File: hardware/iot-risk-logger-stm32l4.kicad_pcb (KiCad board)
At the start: 2 copper layers, 51 x 51 mm, 49 parts, among them J2 Conn_ST_STDC14, J3 USB Type-C, Q1 IRLML6401, U1 STM32L412K8Tx, U2 MMA8452QR1, U3 ST25DV04K, U4 OPT3001DNPR, U5 SHT30-DIS, U6 AT25SF041B-SSHD-T, U7 L78L33ABUTR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

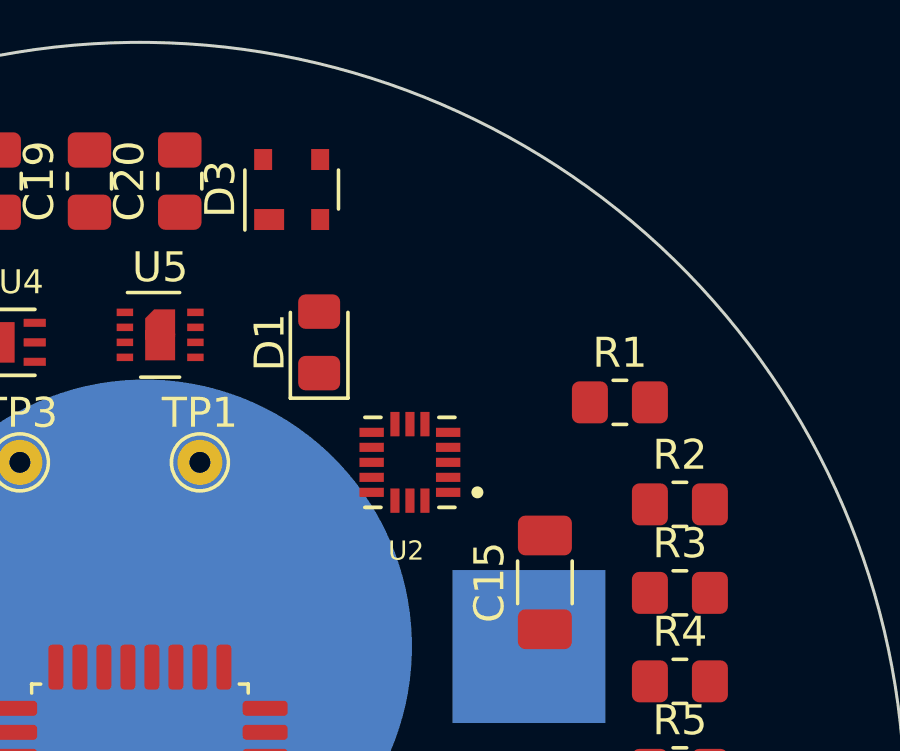
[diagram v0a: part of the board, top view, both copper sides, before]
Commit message: rename to iot-risk-logger-stm32l4 and andd harwware/
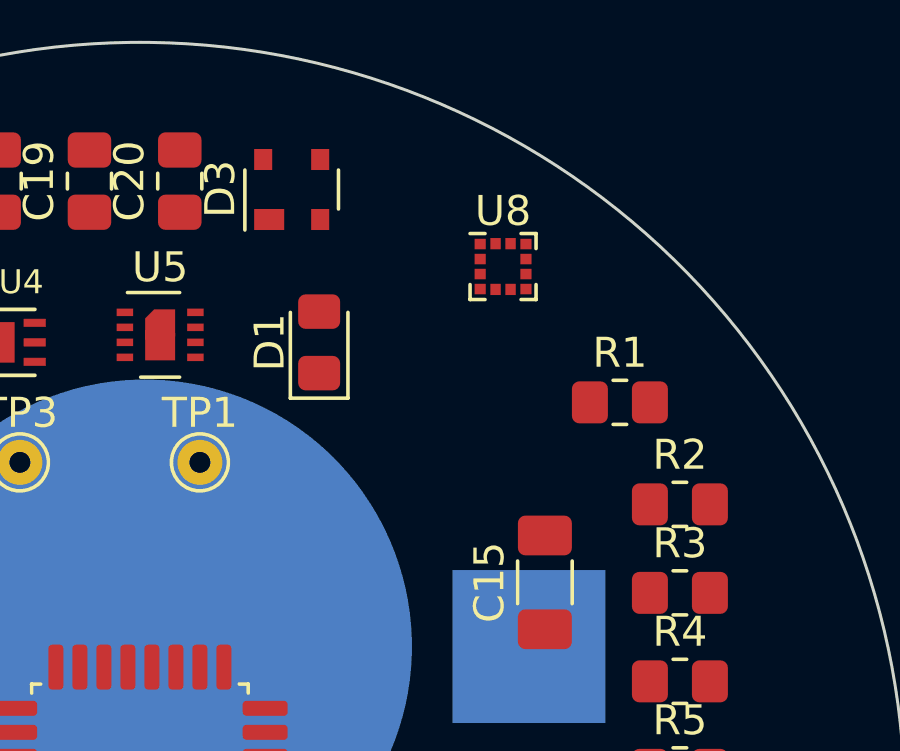
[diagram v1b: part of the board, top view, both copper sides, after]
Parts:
- removed U2: MMA8452QR1, Personal:XDCR_MMA8452QR1
- added U8: LIS2DW12, Package_LGA:LGA-12_2x2mm_P0.5mm, F.Cu at (141.6, 69.0)
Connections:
- C9 pad 1: Net-(U2-BYP) -> unconnected-(C9-Pad1)

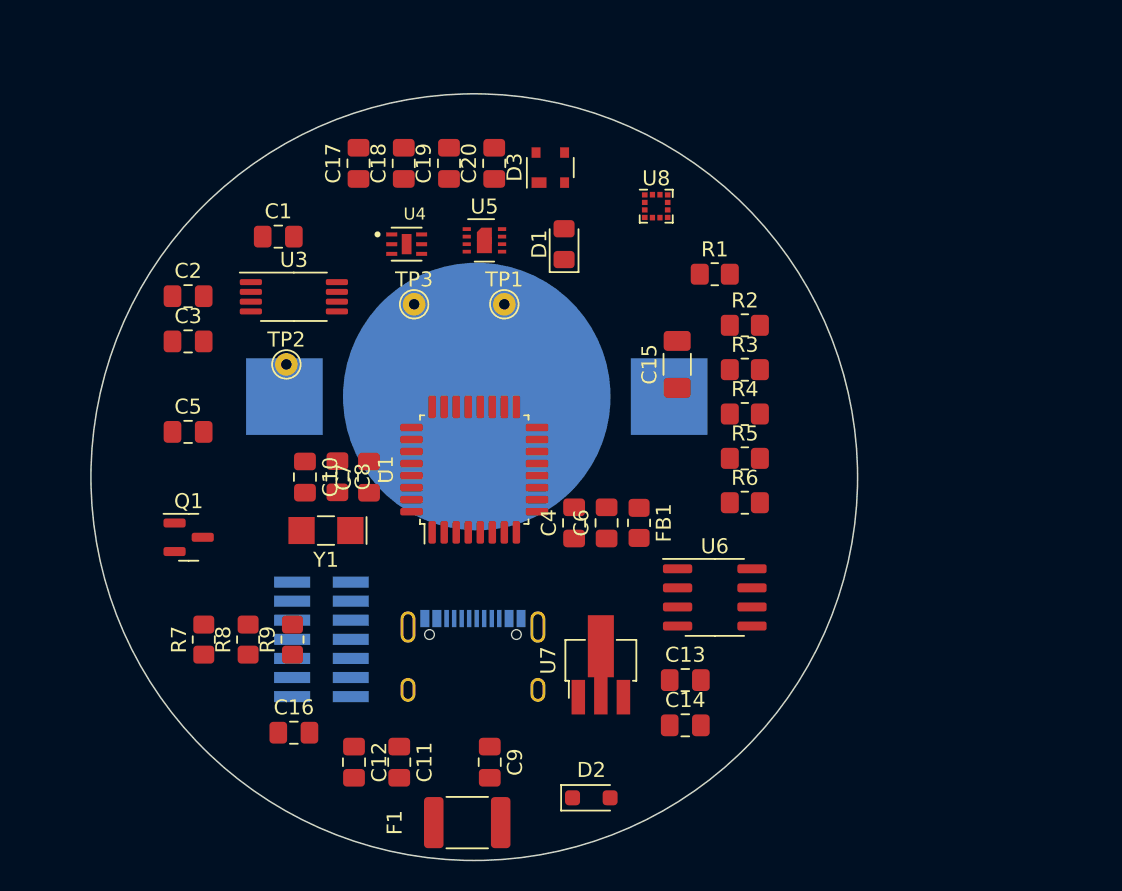
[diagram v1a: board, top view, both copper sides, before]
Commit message: CubeMX: set pins
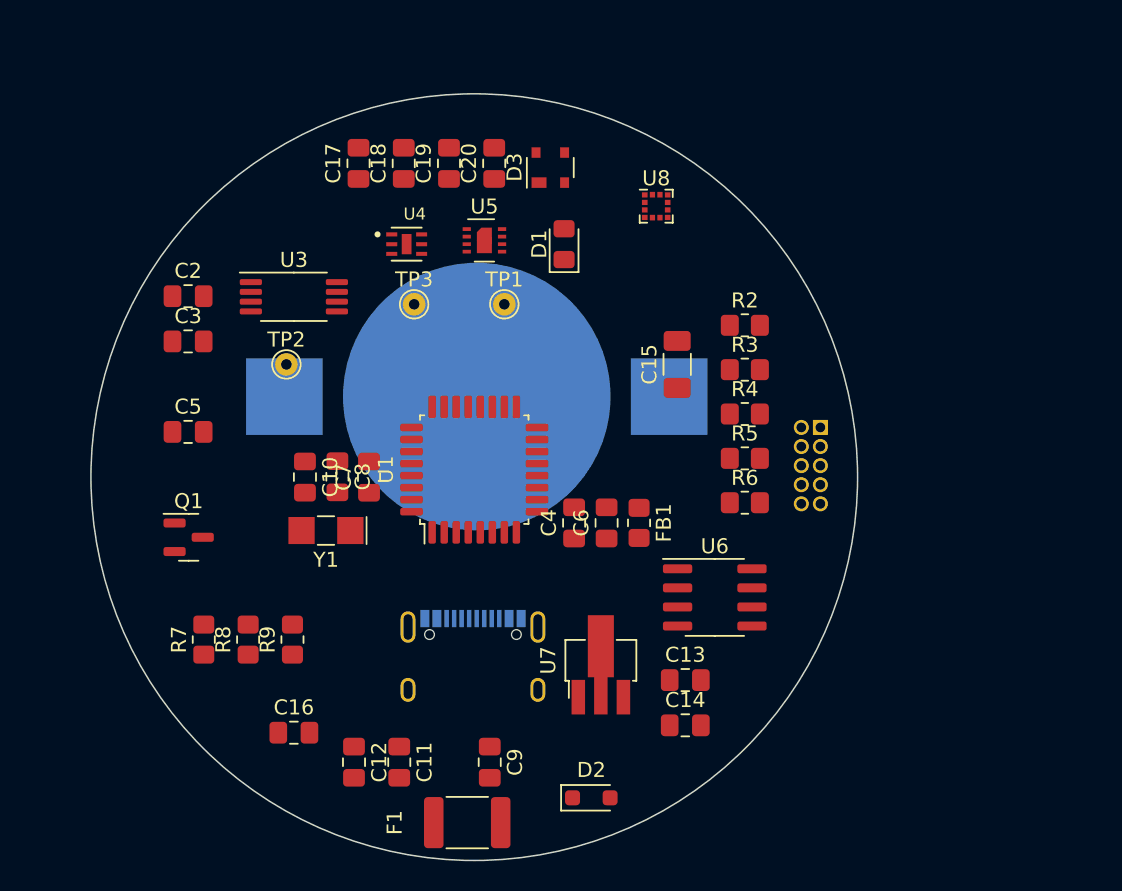
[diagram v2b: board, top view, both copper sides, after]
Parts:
- removed C1: 100n, Capacitor_SMD:C_0805_2012Metric_Pad1.18x1.45mm_HandSolder
- removed J2: Conn_ST_STDC14, Connector_PinHeader_1.27mm:PinHeader_2x07_P1.27mm_Vertical_SMD
- removed R1: 1k, Resistor_SMD:R_0805_2012Metric_Pad1.20x1.40mm_HandSolder
- added J1: Conn_ARM_JTAG_SWD_10, Connector_PinHeader_1.27mm:PinHeader_2x05_P1.27mm_Vertical, B.Cu at (152.5, 83.7)
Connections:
- C17 pad 1: XIN32 -> OSC32_IN
- C18 pad 1: XOUT32 -> OSC32_OUT
- U1 pad 10: unconnected-(U1-PA4-Pad10) -> IMU_INT2
- U1 pad 11: unconnected-(U1-PA5-Pad11) -> SCK
- U1 pad 12: unconnected-(U1-PA6-Pad12) -> MISO
- U1 pad 13: unconnected-(U1-PA7-Pad13) -> MOSI
- U1 pad 14: unconnected-(U1-PB0-Pad14) -> _FLASH_CS
- U1 pad 19: unconnected-(U1-PA9-Pad19) -> SCL
- U1 pad 2: unconnected-(U1-PC14-Pad2) -> OSC32_IN
- U1 pad 20: unconnected-(U1-PA10-Pad20) -> SDA
- U1 pad 21: unconnected-(U1-PA11-Pad21) -> USB_DM
- U1 pad 22: unconnected-(U1-PA12-Pad22) -> USB_DP
- U1 pad 23: unconnected-(U1-PA13-Pad23) -> SWDIO
- U1 pad 24: unconnected-(U1-PA14-Pad24) -> SWDCLK
- U1 pad 26: unconnected-(U1-PB3-Pad26) -> SWO
- U1 pad 3: unconnected-(U1-PC15-Pad3) -> OSC32_OUT
- U1 pad 6: unconnected-(U1-PA0-Pad6) -> _NFC_INT
- U1 pad 7: unconnected-(U1-PA1-Pad7) -> _LIGHT_INT
- U1 pad 8: unconnected-(U1-PA2-Pad8) -> USB_VBUS_SENSE
- U1 pad 9: unconnected-(U1-PA3-Pad9) -> IMU_INT1
- U8 pad 1: unconnected-(U8-SCL/SPC-Pad1) -> SCL
- U8 pad 4: unconnected-(U8-SDA/SDI-Pad4) -> SDA
- Y1 pad 1: XIN32 -> OSC32_IN
- Y1 pad 2: XOUT32 -> OSC32_OUT

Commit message: CubeMX: add qspi
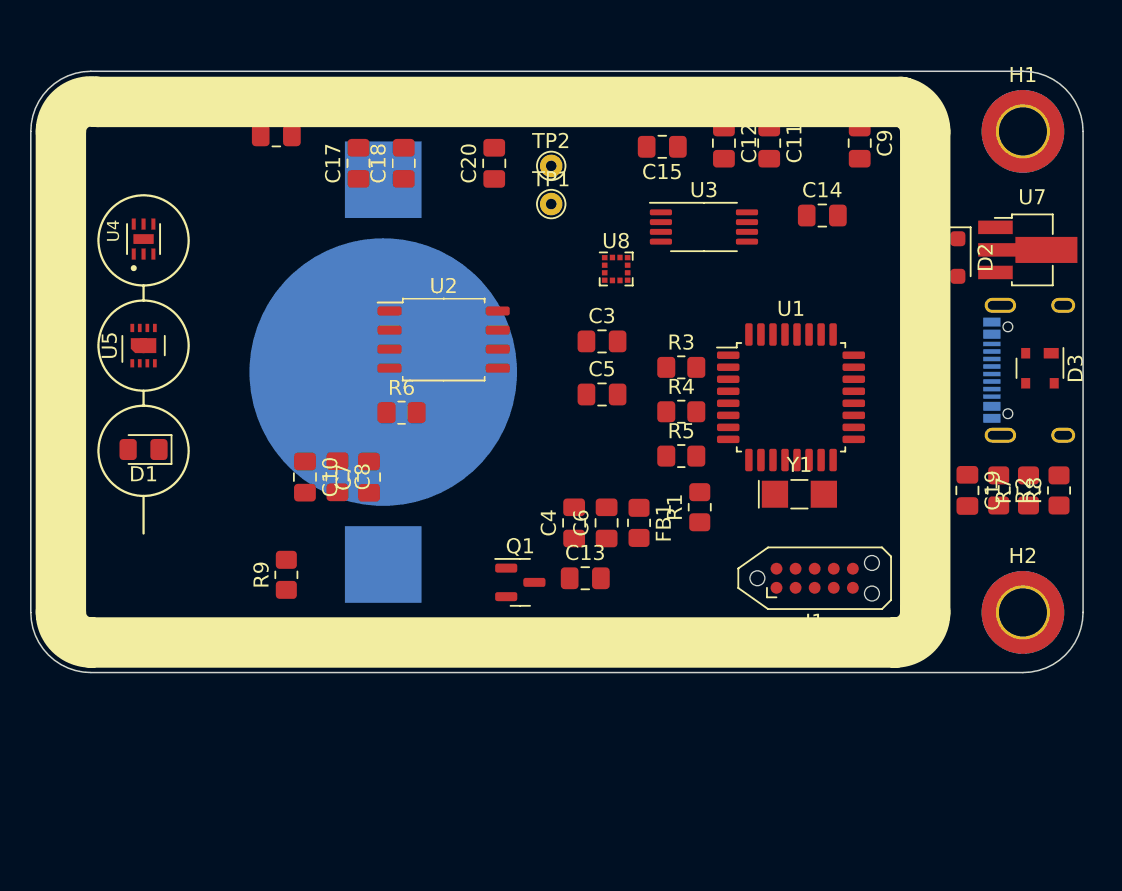
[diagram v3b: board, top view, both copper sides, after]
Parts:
- removed C16: 100n, Capacitor_SMD:C_0805_2012Metric_Pad1.18x1.45mm_HandSolder
- removed F1: MSMF010 0.01A, Fuse:Fuse_1812_4532Metric_Pad1.30x3.40mm_HandSolder
- removed TP3: TestPoint_Probe, TestPoint:TestPoint_THTPad_D1.5mm_Drill0.7mm
- removed U6: AT25SF041B-SSHD-T, Package_SO:SOIC-8_3.9x4.9mm_P1.27mm
- added H1: MountingHole, MountingHole:MountingHole_3.2mm_M3_ISO14580_Pad_TopBottom, F.Cu at (166.0, 64.0)
- added H2: MountingHole, MountingHole:MountingHole_3.2mm_M3_ISO14580_Pad_TopBottom, F.Cu at (166.0, 96.0)
- added R1: 33k, Resistor_SMD:R_0805_2012Metric_Pad1.20x1.40mm_HandSolder, F.Cu at (144.5, 89.0)
- added U2: W25Q64JV, Package_SO:SOIC-8_5.23x5.23mm_P1.27mm, F.Cu at (127.5, 77.9)
- C15: value 22u -> 100n; footprint Capacitor_SMD:C_1206_3216Metric_Pad1.33x1.80mm_HandSolder -> Capacitor_SMD:C_0805_2012Metric_Pad1.18x1.45mm_HandSolder
- C3, C9: value 100n -> 1u
- J1: footprint Connector_PinHeader_1.27mm:PinHeader_2x05_P1.27mm_Vertical -> Connector:Tag-Connect_TC2050-IDC-NL_2x05_P1.27mm_Vertical_with_bottom_clip; moved to F.Cu
- R4, R5: value 4k7 -> 5k1
- R9: value 10k -> 82k
- moved R7 55.8 mm to (166.4, 87.9)
- moved R8 54.9 mm to (168.4, 87.9)
- moved C12 48.0 mm to (146.1, 64.8)
- moved C9 48.0 mm to (155.1, 64.8)
- moved C11 48.0 mm to (149.1, 64.8)
- moved D2 43.4 mm to (161.7, 72.4), turned to -90 degrees
- moved J3 43.2 mm to (167.6, 79.9), turned to -90 degrees
- moved C19 40.8 mm to (162.3, 87.9), turned to -90 degrees
- moved U7 39.6 mm to (166.6, 71.9), turned to 0 degrees
- moved D3 35.2 mm to (167.1, 79.8), turned to -90 degrees
- moved C14 35.1 mm to (152.7, 69.6)
- moved Y1 31.6 mm to (151.1, 88.1), turned to 0 degrees
- moved D1 31.1 mm to (107.5, 85.2), turned to 180 degrees
- moved U3 27.7 mm to (144.8, 70.4)
- moved C5 27.6 mm to (138.0, 81.5)
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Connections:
- net OSC32_IN renamed Net-(U1-PC14)
- net OSC32_OUT renamed Net-(U1-PC15)
- C10 pad 1: /VDDCODE -> /VDDA
- C15 pad 1: +3V0 -> _RESET
- C4 pad 1: /VDDANA -> +3V0
- C6 pad 1: /VDDANA -> +3V0
- C7 pad 1: unconnected-(C7-Pad1) -> +3V0
- C8 pad 1: /VDDCODE -> /VDDA
- C9 pad 1: unconnected-(C9-Pad1) -> +3V0
- FB1 pad 2: /VDDANA -> /VDDA
- Q1 pad 3: Net-(Q1-D) -> Net-(BT1-+)
- R4 pad 2: SDA -> SCL
- R5 pad 2: SCL -> SDA
- R6 pad 1: +5V -> +3V0
- R6 pad 2: USB_VBUS_SENSE -> _QSPI_NCS
- R9 pad 1: USB_VBUS_SENSE -> +5V
- R9 pad 2: GND -> USB_VBUS_SENSE
- U1 pad 1: unconnected-(U1-VDD-Pad1) -> +3V0
- U1 pad 10: IMU_INT2 -> unconnected-(U1-PA4-Pad10)
- U1 pad 11: SCK -> unconnected-(U1-PA5-Pad11)
- U1 pad 12: MISO -> QSPI_IO3
- U1 pad 13: MOSI -> QSPI_IO2
- U1 pad 14: _FLASH_CS -> QSPI_IO1
- U1 pad 15: unconnected-(U1-PB1-Pad15) -> QSPI_IO0
- U1 pad 17: unconnected-(U1-VDD-Pad17) -> +3V0
- U1 pad 18: unconnected-(U1-PA8-Pad18) -> USB_VBUS_SENSE
- U1 pad 25: unconnected-(U1-PA15-Pad25) -> _LED
- U1 pad 27: unconnected-(U1-PB4-Pad27) -> _TEMP_RESET
- U1 pad 28: unconnected-(U1-PB5-Pad28) -> TEMP_INT
- U1 pad 29: unconnected-(U1-PB6-Pad29) -> IMU_INT1
- U1 pad 30: unconnected-(U1-PB7-Pad30) -> IMU_INT2
- U1 pad 5: unconnected-(U1-VDDA-Pad5) -> /VDDA
- U1 pad 8: USB_VBUS_SENSE -> _QSPI_NCS
- U1 pad 9: IMU_INT1 -> QSPI_CLK
- U8 pad 10: unconnected-(U8-Vdd_IO-Pad10) -> +3V0
- U8 pad 5: unconnected-(U8-RES-Pad5) -> GND
- U8 pad 6: Net-(U8-GND-Pad6) -> GND
- U8 pad 7: Net-(U8-GND-Pad6) -> GND
- U8 pad 8: Net-(U8-GND-Pad6) -> GND
- U8 pad 9: unconnected-(U8-Vdd-Pad9) -> +3V0
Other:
- board size 51 x 51 mm -> 70 x 40 mm
- copper layers 2 -> 4
- board text added: "0"
- board text added: "0 mm"
- board text added: "0.0000 mm / 0.0000 mm"
- board text added: "0.01 mm"
- board text added: "0.02"
- board text added: "0.035 mm"
- board text added: "0.1 mm"
- board text added: "0.3000 mm"
- board text added: "1"
- board text added: "1.24 mm"
- board text added: "1.6000 mm"
- board text added: "3.3"
- board text added: "4"
- board text added: "4.5"
- board text added: "70.0000 mm x 40.0000 mm"
- board text added: "B.Cu"
- board text added: "B.Mask"
- board text added: "B.Paste"
- board text added: "B.Silkscreen"
- board text added: "BOARD CHARACTERISTICS"
- board text added: "Board Thickness:"
- board text added: "Board overall dimensions:"
- board text added: "Bottom Silk Screen"
- board text added: "Bottom Solder Mask"
- board text added: "Bottom Solder Paste"
- board text added: "Castellated pads:"
- board text added: "Color"
- board text added: "Copper Finish:"
- board text added: "Copper Layer Count:"
- board text added: "Dielectric 1"
- board text added: "Dielectric 2"
- board text added: "Dielectric 3"
- board text added: "Edge card connectors:"
- board text added: "Epsilon R"
- board text added: "F.Cu"
- board text added: "F.Mask"
- board text added: "F.Paste"
- board text added: "F.Silkscreen"
- board text added: "FR4"
- board text added: "FR4 natural"
- board text added: "Impedance Control:"
- board text added: "In1.Cu"
- board text added: "In2.Cu"
- board text added: "Layer Name"
- board text added: "Loss Tangent"
- board text added: "Material"
- board text added: "Min hole diameter:"
- board text added: "Min track/spacing:"
- board text added: "No"
- board text added: "None"
- board text added: "Not specified"
- board text added: "Plated Board Edge:"
- board text added: "Red"
- board text added: "Thickness (mm)"
- board text added: "Top Silk Screen"
- board text added: "Top Solder Mask"
- board text added: "Top Solder Paste"
- board text added: "Type"
- board text added: "White"
- board text added: "copper"
- board text added: "core"
- board text added: "prepreg"
